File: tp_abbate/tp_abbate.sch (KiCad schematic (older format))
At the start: 45 parts, among them J1 USB_B_Micro, J2 S2B-PH-K-S, J3 U.FL-R-SMT-1(10), J4 Conn_01x12, J5 Conn_01x06, J6 Conn_01x12, Q1 AO3401A, Q2 2N7002, Q3 AO3401A, SW1 SW_Push, SW2 SW_Push, U1 LTC4054ES5-4.2, U2 ESP32-WROOM-32, U3 MIC5219-3.3YMM, U4 Ai-Thinker-Ra-01, U5 CP2102-GM-QFN28

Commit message: Fix comentarios compañero
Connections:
- net GND: now also U5.29 (GND)
- no-connect marks 12 -> 13
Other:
- note added: "Flash button: Driving GPIO0 LOW while\nreset, enters Flash mode"
- note added: "Reset button"
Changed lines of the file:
@@
 L power:GND #PWR042
 U 1 1 5ED8B990
-P 10000 2450
-F 0 "#PWR042" H 10000 2200 50  0001 C CNN
-F 1 "GND" H 10005 2277 50  0000 C CNN
-F 2 "" H 10000 2450 50  0001 C CNN
-F 3 "" H 10000 2450 50  0001 C CNN
-	1    10000 2450
+P 10000 2500
+F 0 "#PWR042" H 10000 2250 50  0001 C CNN
+F 1 "GND" H 10005 2327 50  0000 C CNN
+F 2 "" H 10000 2500 50  0001 C CNN
+F 3 "" H 10000 2500 50  0001 C CNN
+	1    10000 2500
 	1    0    0    -1
 $EndComp
@@
 	8500 2000 8800 2000
 $Comp
-L tp_abbate:2N7002 Q2
-U 1 1 5EEE5CA7
-P 2450 4100
-F 0 "Q2" H 2654 4146 50  0000 L CNN
-F 1 "2N7002" H 2654 4055 50  0000 L CNN
-F 2 "Package_TO_SOT_SMD:SOT-363" H 2650 4025 50  0001 L CIN
-F 3 "" H 2450 4100 50  0001 L CNN
-	1    2450 4100
-	1    0    0    -1
-$EndComp
-$Comp
 L Switch:SW_Push SW1
 U 1 1 5EEE805E
@@
 Wire Wire Line
 	2550 3850 2550 3900
-Text Label 1800 4100 0    50   ~ 0
-DTR
 Wire Wire Line
 	1800 4100 2100 4100
-Text Label 1800 4900 0    50   ~ 0
-RTS
 Wire Wire Line
 	1800 4900 2200 4900
@@
 Wire Wire Line
 	2550 5100 2550 5150
-$Comp
-L tp_abbate:2N7002 Q2
-U 2 1 5EEE69D9
-P 2450 4900
-F 0 "Q2" H 2654 4854 50  0000 L CNN
-F 1 "2N7002" H 2654 4945 50  0000 L CNN
-F 2 "Package_TO_SOT_SMD:SOT-363" H 2650 4825 50  0001 L CIN
-F 3 "" H 2450 4900 50  0001 L CNN
-	2    2450 4900
-	1    0    0    1
-$EndComp
 Wire Wire Line
 	2550 4700 2550 4500
@@
 	1200 2200 1200 2150
 Wire Wire Line
-	4700 1700 5250 1700
+	4700 1700 5000 1700
 Wire Wire Line
 	3850 2450 3900 2450
@@
 Text Notes 4050 2900 0    50   ~ 0
 Close to\nboard edge.\nBattery connector
+NoConn ~ 1550 1350
+$Comp
+L power:PWR_FLAG #FLG0101
+U 1 1 5EE18886
+P 5000 1600
+F 0 "#FLG0101" H 5000 1675 50  0001 C CNN
+F 1 "PWR_FLAG" H 5000 1773 50  0000 C CNN
+F 2 "" H 5000 1600 50  0001 C CNN
+F 3 "~" H 5000 1600 50  0001 C CNN
+	1    5000 1600
+	1    0    0    -1
+$EndComp
+Wire Wire Line
+	5000 1600 5000 1700
+Connection ~ 5000 1700
+Wire Wire Line
+	5000 1700 5250 1700
+$Comp
+L power:PWR_FLAG #FLG0102
+U 1 1 5EE25AE8
+P 3500 750
+F 0 "#FLG0102" H 3500 825 50  0001 C CNN
+F 1 "PWR_FLAG" H 3500 923 50  0000 C CNN
+F 2 "" H 3500 750 50  0001 C CNN
+F 3 "~" H 3500 750 50  0001 C CNN
+	1    3500 750
+	1    0    0    -1
+$EndComp
+Wire Wire Line
+	3500 750  3500 950
+Wire Wire Line
+	9900 2400 9900 2450
+Wire Wire Line
+	9900 2450 10000 2450
+Connection ~ 10000 2450
+Wire Wire Line
+	10000 2450 10000 2500
+Text Notes 1750 3550 0    50   ~ 0
+Reset button
+Wire Notes Line
+	1350 3800 1750 3550
+Wire Notes Line
+	1300 5200 1500 5350
+Text Label 1800 4100 0    50   ~ 0
+DTR
+$Comp
+L tp_abbate:2N7002 Q2
+U 2 1 5EEE69D9
+P 2450 4900
+F 0 "Q2" H 2654 4854 50  0000 L CNN
+F 1 "2N7002" H 2654 4945 50  0000 L CNN
+F 2 "Package_TO_SOT_SMD:SOT-363" H 2650 4825 50  0001 L CIN
+F 3 "" H 2450 4900 50  0001 L CNN
+	2    2450 4900
+	1    0    0    1
+$EndComp
+Text Label 1800 4900 0    50   ~ 0
+RTS
+$Comp
+L tp_abbate:2N7002 Q2
+U 1 1 5EEE5CA7
+P 2450 4100
+F 0 "Q2" H 2654 4146 50  0000 L CNN
+F 1 "2N7002" H 2654 4055 50  0000 L CNN
+F 2 "Package_TO_SOT_SMD:SOT-363" H 2650 4025 50  0001 L CIN
+F 3 "" H 2450 4100 50  0001 L CNN
+	1    2450 4100
+	1    0    0    -1
+$EndComp
+Text Notes 1500 5450 0    50   ~ 0
+Flash button: Driving GPIO0 LOW while\nreset, enters Flash mode
 $EndSCHEMATC

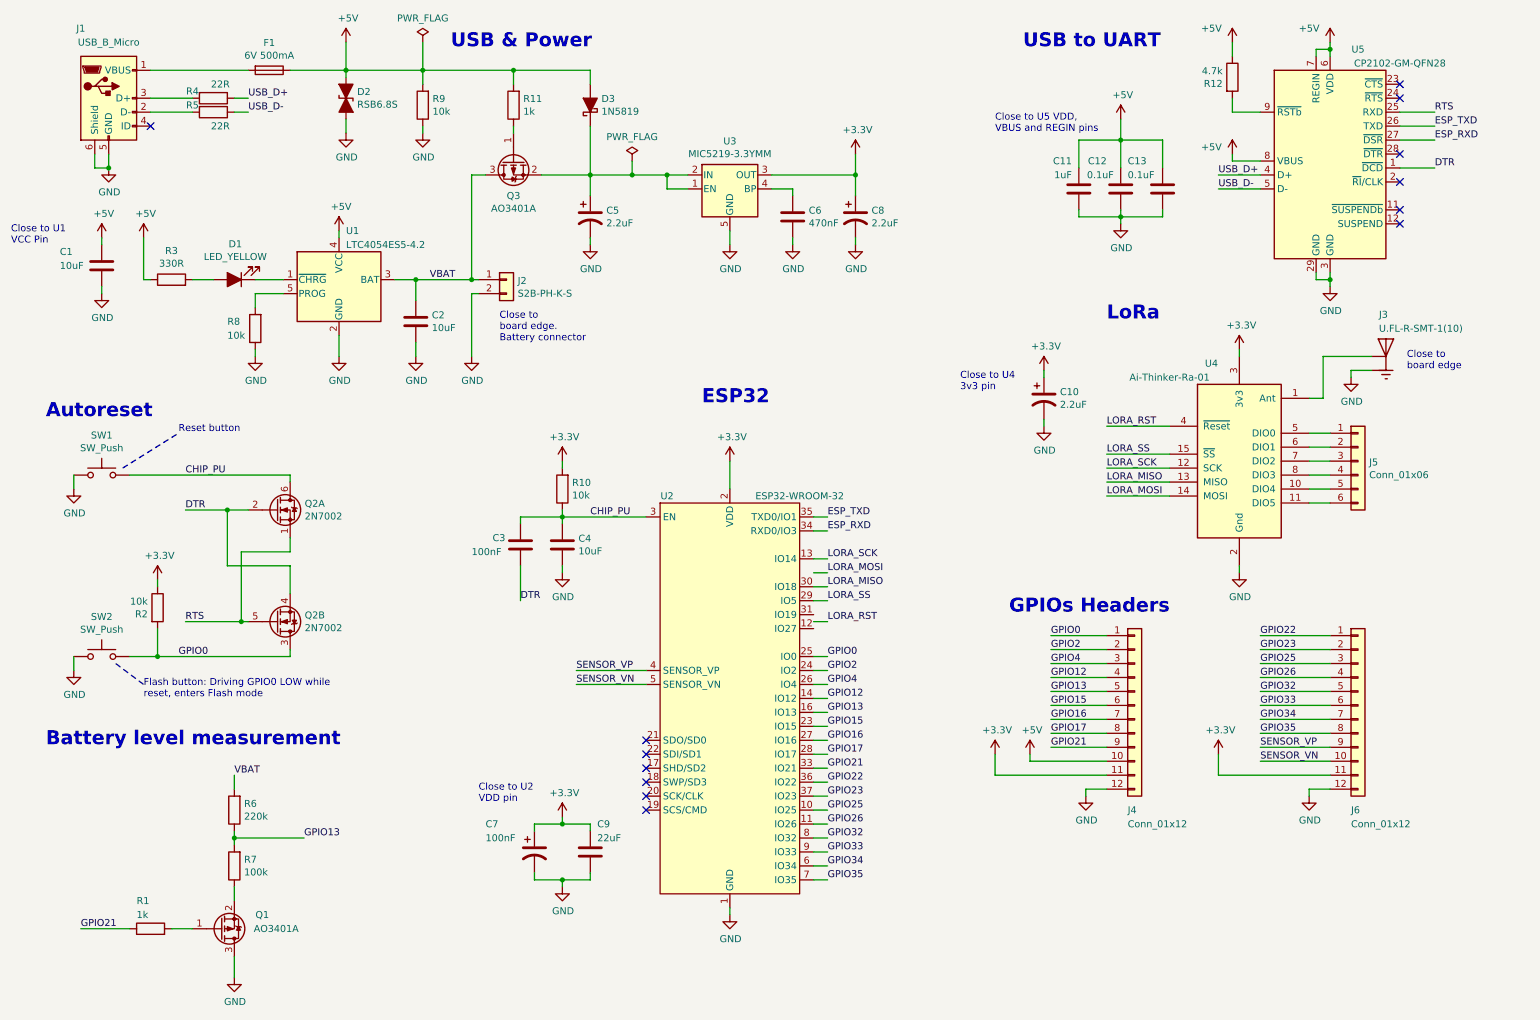
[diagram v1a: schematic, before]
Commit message: Trabajo en PCB - ubicacion de componentes
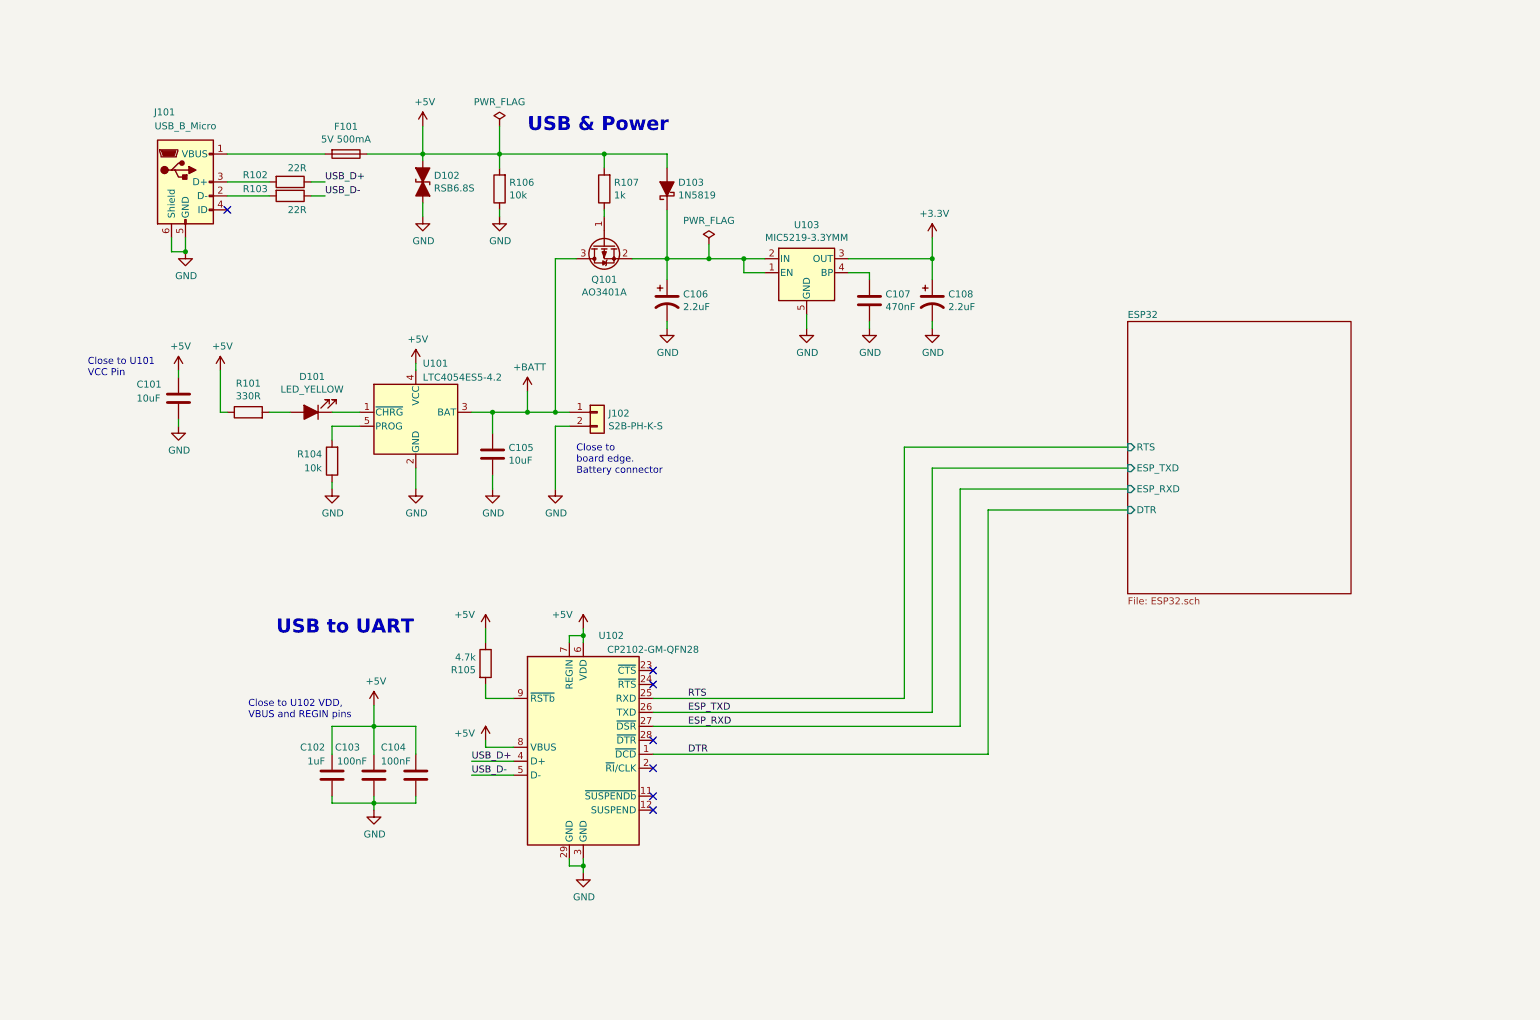
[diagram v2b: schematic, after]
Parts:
- removed C10: 2.2uF, symbol Device:CP1
- removed C3, C9: 100nF, symbol Device:C
- removed C4: 10uF, symbol Device:C
- removed C7: 22uF, symbol Device:CP1
- removed J3: U.FL-R-SMT-1(10), HRS_U.FL-R-SMT-1(10), symbol tp_abbate:U.FL-R-SMT-1(10)
- removed J4, J6: Conn_01x12, symbol Connector_Generic:Conn_01x12
- removed J5: Conn_01x06, symbol Connector_Generic:Conn_01x06
- removed Q1: AO3401A, Package_TO_SOT_SMD:SOT-23, symbol Transistor_FET:AO3401A
- removed Q2: 2N7002, Package_TO_SOT_SMD:SOT-363, symbol tp_abbate:2N7002
- removed R1: 1k, symbol Device:R
- removed R10, R2: 10k, symbol Device:R
- removed R6: 220k, symbol Device:R
- removed R7: 100k, symbol Device:R
- removed SW1, SW2: SW_Push, symbol Switch:SW_Push
- removed U2: ESP32-WROOM-32, RF_Module:ESP32-WROOM-32, symbol tp_abbate:ESP32-WROOM-32
- removed U4: Ai-Thinker-Ra-01, RF_Module:Ai-Thinker-Ra-01-LoRa, symbol tp_abbate:Ai-Thinker-Ra-01
- C101: renamed from C1; footprint (none) -> Capacitor_Tantalum_SMD:CP_EIA-2012-12_Kemet-R_Pad1.30x1.05mm_HandSolder; Desc (none) -> 10µF Molded Tantalum Capacitors 16V 0805 (2012 Metric) 4Ohm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; Digikey# (none) -> 478-F981C106MSUAJ6CT-ND; Manf (none) -> AVX Corporation
- C102: renamed from C11; footprint (none) -> Capacitor_Tantalum_SMD:CP_EIA-3216-10_Kemet-I_Pad1.58x1.35mm_HandSolder; Desc (none) -> 1µF Molded Tantalum Capacitors 25V 1206 (3216 Metric); Digikey# (none) -> 511-TCA1E105M8RCT-ND; Manf (none) -> Rohm Semiconductor
- C103: renamed from C12; value 0.1uF -> 100nF; footprint (none) -> Capacitor_SMD:C_0805_2012Metric_Pad1.15x1.40mm_HandSolder; Desc (none) -> 0.1µF -20%, +80% 50V Ceramic Capacitor Y5V (F) 0805 (2012 M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; Digikey# (none) -> 399-1177-1-ND; Manf (none) -> KEMET
- C104: renamed from C13; value 0.1uF -> 100nF; footprint (none) -> Capacitor_SMD:C_0805_2012Metric_Pad1.15x1.40mm_HandSolder; Desc (none) -> 0.1µF -20%, +80% 50V Ceramic Capacitor Y5V (F) 0805 (2012 M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; Digikey# (none) -> 399-1177-1-ND; Manf (none) -> KEMET
- C105: renamed from C2; footprint (none) -> Capacitor_Tantalum_SMD:CP_EIA-2012-12_Kemet-R_Pad1.30x1.05mm_HandSolder; Desc (none) -> 10µF Molded Tantalum Capacitors 16V 0805 (2012 Metric) 4Ohm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; Digikey# (none) -> 478-F981C106MSUAJ6CT-ND; Manf (none) -> AVX Corporation
- C106: renamed from C5; footprint (none) -> Capacitor_Tantalum_SMD:CP_EIA-3216-18_Kemet-A_Pad1.58x1.35mm_HandSolder; Desc (none) -> 2.2µF Molded Tantalum Capacitors 10V 1206 (3216 Metric) 7Oh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; Digikey# (none) -> TAJA225M010SNJ; Manf (none) -> AVX Corporation
- C107: renamed from C6; footprint (none) -> Capacitor_SMD:C_0805_2012Metric_Pad1.15x1.40mm_HandSolder; Desc (none) -> 0.47µF -20%, +80% 16V Ceramic Capacitor Y5V (F) 0805 (2012 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; Digikey# (none) -> 311-4355-1-ND; Manf (none) -> Yageo
- C108: renamed from C8; footprint (none) -> Capacitor_Tantalum_SMD:CP_EIA-3216-18_Kemet-A_Pad1.58x1.35mm_HandSolder; Desc (none) -> 2.2µF Molded Tantalum Capacitors 10V 1206 (3216 Metric) 7Oh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; Digikey# (none) -> TAJA225M010SNJ; Manf (none) -> AVX Corporation
- D101: renamed from D1; footprint (none) -> LED_SMD:LED_0805_2012Metric_Pad1.15x1.40mm_HandSolder
- D102: renamed from D2; footprint (none) -> Diode_SMD:D_SOD-523; Desc (none) -> TVS DIODE 3.5V EMD2; Digikey# (none) -> RSB6.8STE61TR-ND; Manf (none) -> Rohm Semiconductor
- D103: renamed from D3; footprint (none) -> Diode_SMD:D_SOD-123; Desc (none) -> Diode Schottky 40V 1A Surface Mount SOD-123; Digikey# (none) -> 1N5819HW-FDICT-ND; Manf (none) -> Diodes Incorporated
- F101: renamed from F1; value 6V 500mA -> 5V 500mA; footprint (none) -> Fuse:Fuse_0603_1608Metric_Pad1.05x0.95mm_HandSolder; Desc (none) -> 500mA AC 5V DC Fuse Board Mount (Cartridge Style Excluded) 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; Digikey# (none) -> F12131CT-ND; Manf (none) -> Littelfuse Inc.
- J101: renamed from J1; footprint (none) -> Connector_USB:USB_Micro-B_Molex_47346-0001; Desc (none) -> CONN RCPT USB2.0 MICRO B SMD R/A; Digikey# (none) -> WM17141CT-ND; Manf (none) -> Molex
- J102: renamed from J2; footprint (none) -> Connector_JST:JST_PH_S2B-PH-K_1x02_P2.00mm_Horizontal; Desc (none) -> Connector Header Through Hole, Right Angle 2 position 0.079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; Digikey# (none) -> 455-1719-ND; Manf (none) -> JST Sales America Inc.
- Q101: renamed from Q3; Desc (none) -> MOSFET P-CH 30V 4A SOT23; Digikey# (none) -> 785-1001-6-ND; Manf (none) -> Alpha & Omega Semiconductor Inc.
- R101: renamed from R3; footprint (none) -> Resistor_SMD:R_0805_2012Metric_Pad1.15x1.40mm_HandSolder
- R102: renamed from R4; footprint (none) -> Resistor_SMD:R_0805_2012Metric_Pad1.15x1.40mm_HandSolder
- R103: renamed from R5; footprint (none) -> Resistor_SMD:R_0805_2012Metric_Pad1.15x1.40mm_HandSolder
- R104: renamed from R8; footprint (none) -> Resistor_SMD:R_0805_2012Metric_Pad1.15x1.40mm_HandSolder
- R105: renamed from R12; footprint (none) -> Resistor_SMD:R_0805_2012Metric_Pad1.15x1.40mm_HandSolder
- R106: renamed from R9; footprint (none) -> Resistor_SMD:R_0805_2012Metric_Pad1.15x1.40mm_HandSolder
- R107: renamed from R11; footprint (none) -> Resistor_SMD:R_0805_2012Metric_Pad1.15x1.40mm_HandSolder
- U101: renamed from U1; Desc (none) -> IC CHARGR BATTERY L-ION TSOT23-5; Digikey# (none) -> LTC4054ES5-4.2#TRMPBFTR-ND; Manf (none) -> Linear Technology/Analog Devices
- U102: renamed from U5; Desc (none) -> IC USB TO UART BRIDGE QFN28; Digikey# (none) -> 336-5890-2-ND; Manf (none) -> Silicon Labs
- U103: renamed from U3; Desc (none) -> IC REG LINEAR 3.3V 500MA 8MSOP; Digikey# (none) -> MIC5219-3.3YMM-TR-ND; Manf (none) -> Microchip Technology
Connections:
- net VBAT renamed +BATT
- no-connect marks 13 -> 7
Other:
- note added: "Close to U101\nVCC Pin"
- note added: "Close to U102 VDD,\nVBUS and REGIN pins\n"
- note removed: "Autoreset"
- note removed: "Battery level measurement"
- note removed: "Close to U1\nVCC Pin"
- note removed: "Close to U2\nVDD pin\n"
- note removed: "Close to U4\n3v3 pin\n"
- note removed: "Close to U5 VDD,\nVBUS and REGIN pins\n"
- note removed: "Close to\nboard edge"
- note removed: "ESP32"
- note removed: "Flash button: Driving GPIO0 LOW while\nreset, enters Flash mode"
- note removed: "GPIOs Headers"
- note removed: "LoRa"
- note removed: "Reset button"
- moved on the sheet: C101, C102, C103, C104, C105, C106, C107, C108, D101, D102, D103, F101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

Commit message: WIP revisión PCB
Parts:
- added FID1, FID2, FID3: Fiducial, Fiducial:Fiducial_0.5mm_Mask1.5mm, symbol Mechanical:Fiducial
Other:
- note added: "Place on Front Layer.\nBack Layer will be hand soldered."
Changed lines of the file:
@@
 Wire Wire Line
 	5150 5550 7150 5550
+$Comp
+L Mechanical:Fiducial FID1
+U 1 1 5EF2822C
+P 10150 1050
+F 0 "FID1" H 10235 1096 50  0000 L CNN
+F 1 "Fiducial" H 10235 1005 50  0000 L CNN
+F 2 "Fiducial:Fiducial_0.5mm_Mask1.5mm" H 10150 1050 50  0001 C CNN
+F 3 "~" H 10150 1050 50  0001 C CNN
+	1    10150 1050
+	1    0    0    -1
+$EndComp
+$Comp
+L Mechanical:Fiducial FID2
+U 1 1 5EF29081
+P 10150 1300
+F 0 "FID2" H 10235 1346 50  0000 L CNN
+F 1 "Fiducial" H 10235 1255 50  0000 L CNN
+F 2 "Fiducial:Fiducial_0.5mm_Mask1.5mm" H 10150 1300 50  0001 C CNN
+F 3 "~" H 10150 1300 50  0001 C CNN
+	1    10150 1300
+	1    0    0    -1
+$EndComp
+$Comp
+L Mechanical:Fiducial FID3
+U 1 1 5EF29733
+P 10150 1550
+F 0 "FID3" H 10235 1596 50  0000 L CNN
+F 1 "Fiducial" H 10235 1505 50  0000 L CNN
+F 2 "Fiducial:Fiducial_0.5mm_Mask1.5mm" H 10150 1550 50  0001 C CNN
+F 3 "~" H 10150 1550 50  0001 C CNN
+	1    10150 1550
+	1    0    0    -1
+$EndComp
+Text Notes 9850 1900 0    50   ~ 0
+Place on Front Layer.\nBack Layer will be hand soldered.
 $EndSCHEMATC

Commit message: Subo PCB para revisión compañero
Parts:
- renumbered C101 to C1, C102 to C2, C103 to C3, C104 to C4, C105 to C5, C106 to C6, C107 to C7, C108 to C8, D101 to D1, D102 to D2, D103 to D3, F101 to F1, J101 to J1, J102 to J2, Q101 to Q1, R101 to R1, R102 to R2, R103 to R3, R104 to R4, R105 to R5, R106 to R6, R107 to R7, U101 to U1, U102 to U2, U103 to U3
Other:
- note added: "Close to U2 VDD,\nVBUS and REGIN pins\n"
- note removed: "Close to U102 VDD,\nVBUS and REGIN pins\n"
- moved on the sheet: FID1, FID2, FID3

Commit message: Corrijo indicaciones de compañero
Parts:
- removed C2: 1uF, Capacitor_Tantalum_SMD:CP_EIA-3216-10_Kemet-I_Pad1.58x1.35mm_HandSolder, symbol Device:C
- added C2: 1uF, Capacitor_Tantalum_SMD:CP_EIA-3216-10_Kemet-I_Pad1.58x1.35mm_HandSolder, symbol Device:CP1
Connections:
- net +5V: now also C2.1
- net GND: now also C2.2
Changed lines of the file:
@@
-$EndComp
-$Comp
-L Device:C C2
-U 1 1 5ED9725D
-P 2850 6000
-F 0 "C2" H 2900 5800 50  0000 L CNN
-F 1 "1uF" H 2900 5900 50  0000 L CNN
-F 2 "Capacitor_Tantalum_SMD:CP_EIA-3216-10_Kemet-I_Pad1.58x1.35mm_HandSolder" H 2888 5850 50  0001 C CNN
-F 3 "~" H 2850 6000 50  0001 C CNN
-F 4 "1µF Molded Tantalum Capacitors 25V 1206 (3216 Metric)" H 2850 6000 50  0001 C CNN "Desc"
-F 5 "511-TCA1E105M8RCT-ND" H 2850 6000 50  0001 C CNN "Digikey#"
-F 6 "Rohm Semiconductor" H 2850 6000 50  0001 C CNN "Manf"
-	1    2850 6000
-	-1   0    0    1
 $EndComp
 $Comp
@@
 Text Notes 9650 1950 0    50   ~ 0
 Place on Front Layer.\nBack Layer will be hand soldered.
+$Comp
+L Device:CP1 C2
+U 1 1 5EF72A03
+P 2850 6000
+F 0 "C2" H 2600 6200 50  0000 L CNN
+F 1 "1uF" H 2600 6100 50  0000 L CNN
+F 2 "Capacitor_Tantalum_SMD:CP_EIA-3216-10_Kemet-I_Pad1.58x1.35mm_HandSolder" H 2850 6000 50  0001 C CNN
+F 3 "~" H 2850 6000 50  0001 C CNN
+F 4 "1µF Molded Tantalum Capacitors 25V 1206 (3216 Metric)" H 2850 6000 50  0001 C CNN "Desc"
+F 5 "511-TCA1E105M8RCT-ND" H 2850 6000 50  0001 C CNN "Digikey#"
+F 6 "Rohm Semiconductor" H 2850 6000 50  0001 C CNN "Manf"
+	1    2850 6000
+	1    0    0    -1
+$EndComp
 $EndSCHEMATC

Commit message: Revisión Final - Entrega
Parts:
- added H1, H2, H3, H4: MountingHole, tp_abbate:MountingHole_1.8mm_M3, symbol Mechanical:MountingHole
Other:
- note added: "Mounting holes.\nDia. 3.2 mm"
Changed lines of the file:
@@
 	1    0    0    -1
 $EndComp
+$Comp
+L Mechanical:MountingHole H1
+U 1 1 5EFBB7A6
+P 8500 1100
+F 0 "H1" H 8600 1100 50  0000 L CNN
+F 1 "MountingHole" H 8600 1055 50  0001 L CNN
+F 2 "tp_abbate:MountingHole_1.8mm_M3" H 8500 1100 50  0001 C CNN
+F 3 "~" H 8500 1100 50  0001 C CNN
+	1    8500 1100
+	1    0    0    -1
+$EndComp
+$Comp
+L Mechanical:MountingHole H2
+U 1 1 5EFBC4FA
+P 8900 1100
+F 0 "H2" H 9000 1100 50  0000 L CNN
+F 1 "MountingHole" H 9000 1055 50  0001 L CNN
+F 2 "tp_abbate:MountingHole_1.8mm_M3" H 8900 1100 50  0001 C CNN
+F 3 "~" H 8900 1100 50  0001 C CNN
+	1    8900 1100
+	1    0    0    -1
+$EndComp
+$Comp
+L Mechanical:MountingHole H3
+U 1 1 5EFBC92C
+P 8500 1350
+F 0 "H3" H 8600 1350 50  0000 L CNN
+F 1 "MountingHole" H 8600 1305 50  0001 L CNN
+F 2 "tp_abbate:MountingHole_1.8mm_M3" H 8500 1350 50  0001 C CNN
+F 3 "~" H 8500 1350 50  0001 C CNN
+	1    8500 1350
+	1    0    0    -1
+$EndComp
+$Comp
+L Mechanical:MountingHole H4
+U 1 1 5EFBCDE8
+P 8900 1350
+F 0 "H4" H 9000 1350 50  0000 L CNN
+F 1 "MountingHole" H 9000 1305 50  0001 L CNN
+F 2 "tp_abbate:MountingHole_1.8mm_M3" H 8900 1350 50  0001 C CNN
+F 3 "~" H 8900 1350 50  0001 C CNN
+	1    8900 1350
+	1    0    0    -1
+$EndComp
+Text Notes 8450 1700 0    50   ~ 0
+Mounting holes.\nDia. 3.2 mm
 $EndSCHEMATC
